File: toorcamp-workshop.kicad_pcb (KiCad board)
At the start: 2 copper layers, 101.6 x 50.8 mm, 13 parts

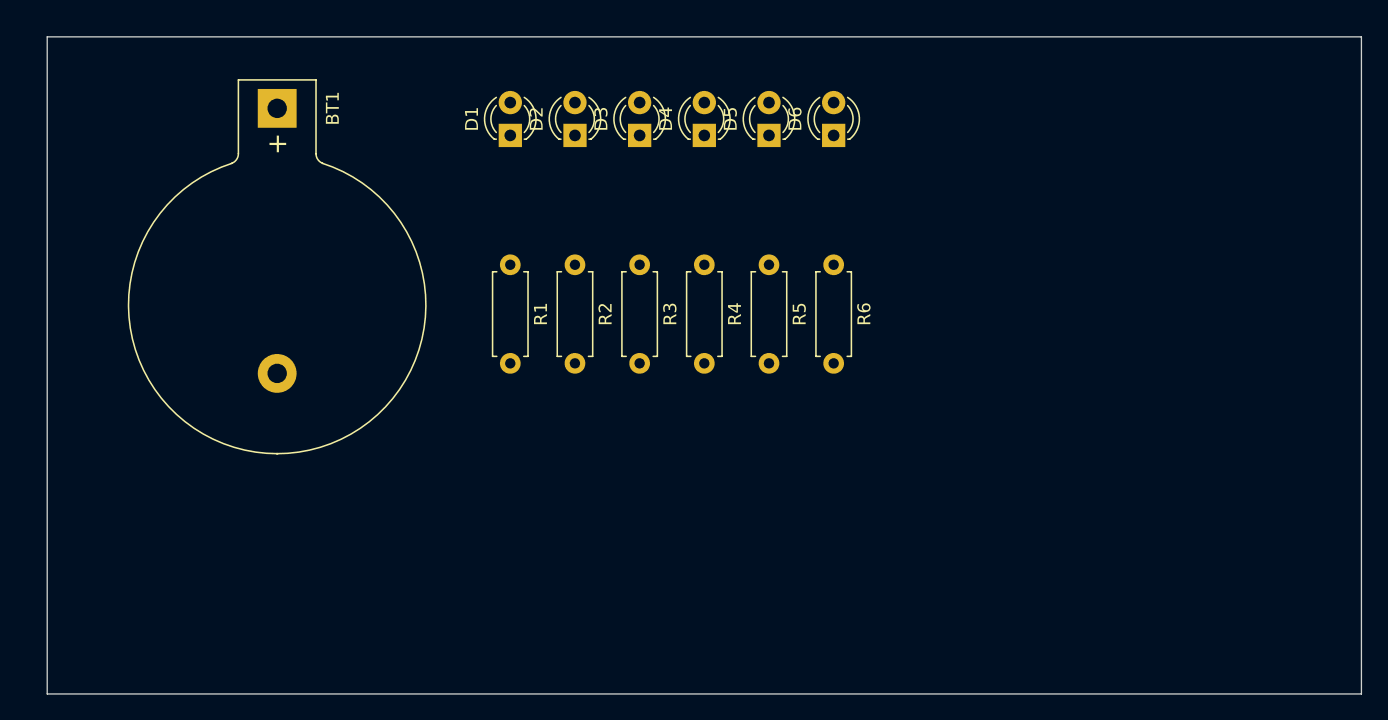
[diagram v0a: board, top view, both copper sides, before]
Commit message: adjust default dimensions
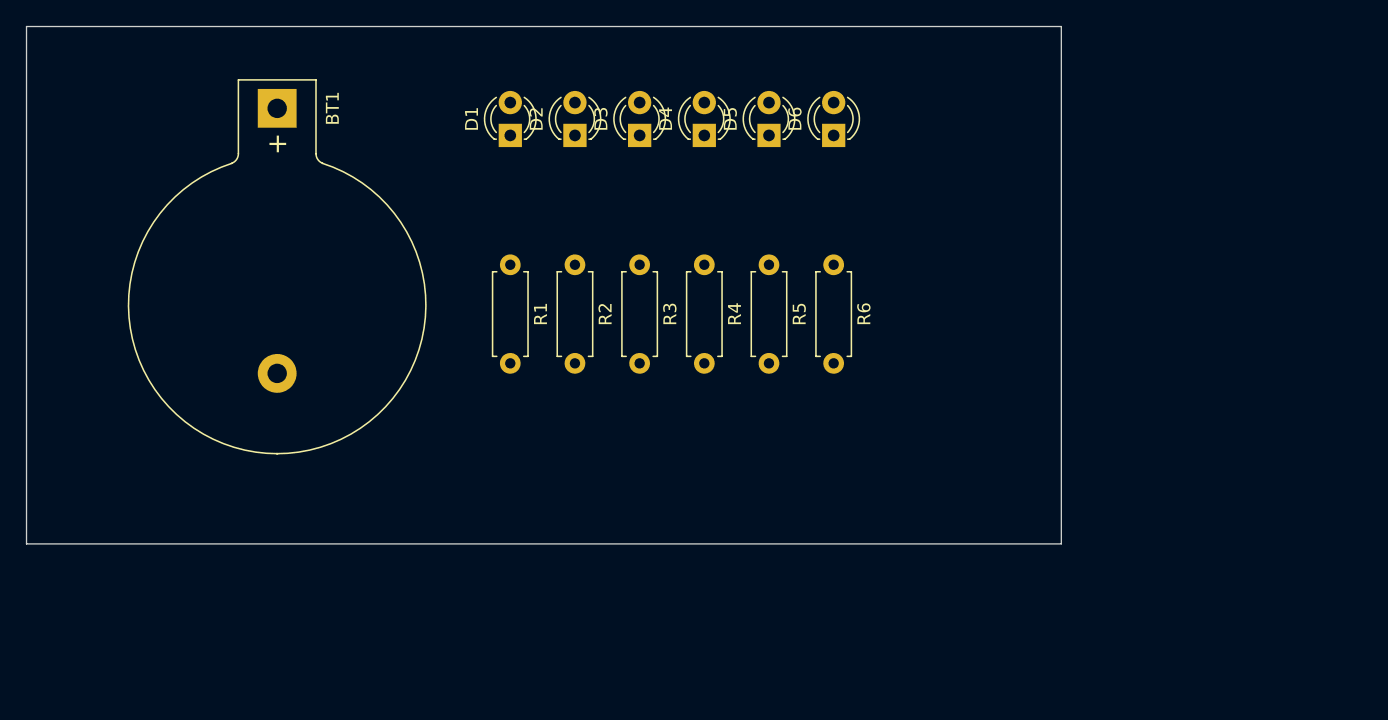
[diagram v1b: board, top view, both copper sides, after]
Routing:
- net Net-(BT1-Pad2): track 0.00 -> 1.10 mm
- net Net-(BT1-Pad1): track 0.00 -> 0.63 mm
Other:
- board size 101.6 x 50.8 mm -> 80 x 40 mm
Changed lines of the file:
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@@
     )
   )
-  (gr_rect (start 101.6 50.8) (end 203.2 101.6) (layer "Edge.Cuts") (width 0.1) (fill none))
+  (gr_rect (start 100 50) (end 180 90) (layer "Edge.Cuts") (width 0.1) (fill none))
+  (segment (start 119.827584 55.88) (end 119.38 56.327584) (width 0.25) (layer "F.Cu") (net 1))
+  (segment (start 120.157584 76.04) (end 119.38 76.817584) (width 0.25) (layer "F.Cu") (net 2))
+  (segment (start 137.4 58.42) (end 137.4 58.66) (width 0.25) (layer "F.Cu") (net 3))
 )
